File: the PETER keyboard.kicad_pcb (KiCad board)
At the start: 2 copper layers, 241.6 x 96.9 mm, 141 parts, among them J1 USB_C_Receptacle_USB2.0, SW1 RotaryEncoder_Switch, SW12 RotaryEncoder_Switch, SW2 SW_Push, U1 ATmega32U4-M, Y1 Crystal_GND24_Small

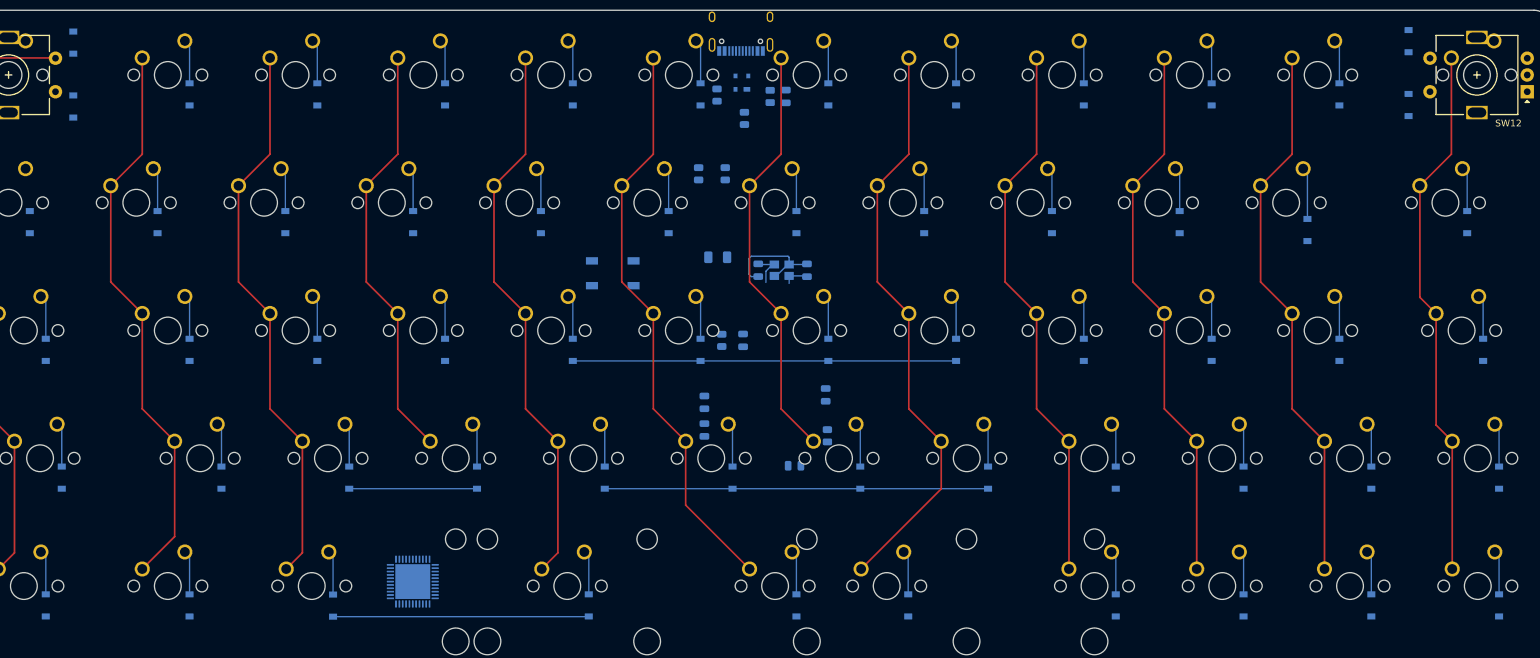
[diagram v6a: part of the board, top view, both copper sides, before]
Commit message: placed MCU and USB for automatic routing
also assigned row and col to MCU
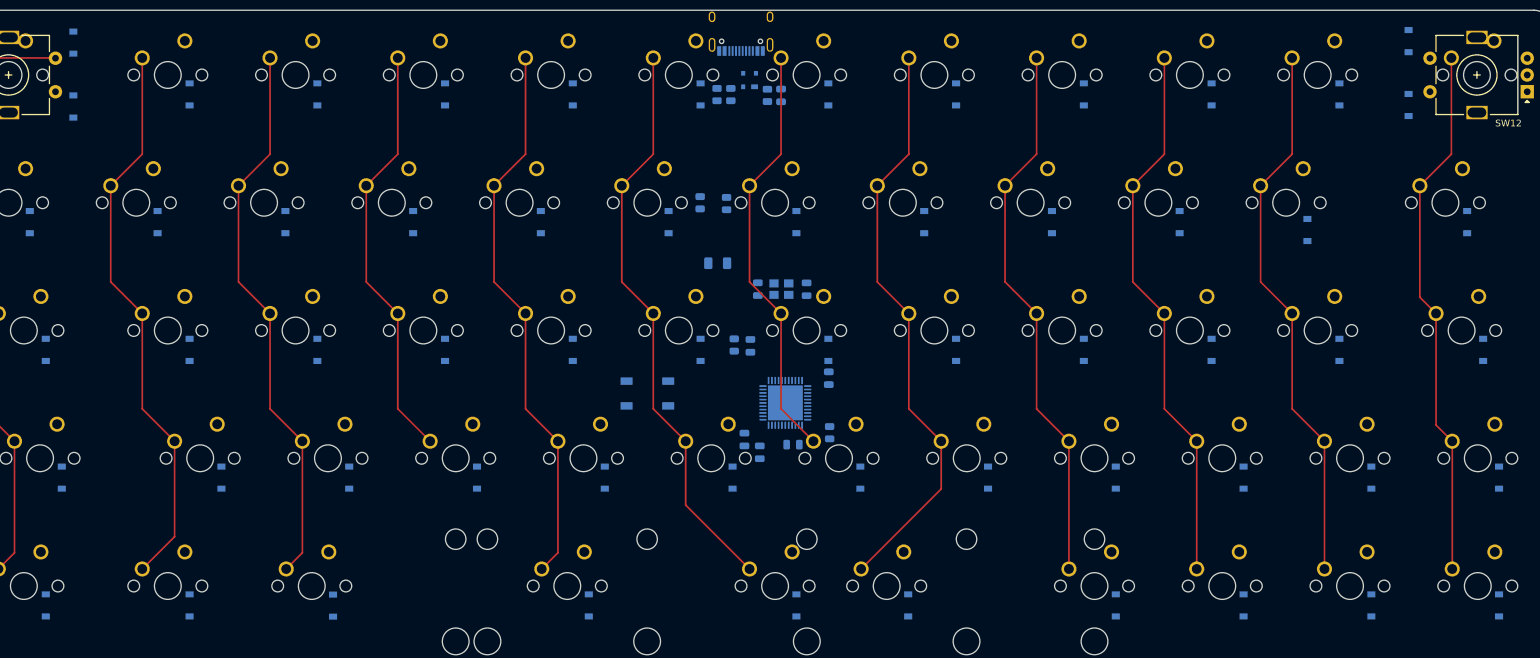
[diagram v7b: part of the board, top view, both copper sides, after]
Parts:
- moved U1 61.6 mm to (150.7, 105.5)
- moved SW2 18.7 mm to (130.2, 104.1)
- moved C_Decoupler4 8.90 mm to (146.9, 112.9)
- moved C_UCAP1 8.14 mm to (144.7, 111.0)
- moved R_USB4 4.45 mm to (142.0, 75.8)
- moved R_USB3 4.32 mm to (138.0, 75.7)
- moved R_USB2 4.10 mm to (142.6, 59.6)
- moved C_Decoupler2 3.16 mm to (151.9, 111.8)
- moved C_crystal2 2.83 mm to (146.7, 88.6)
- moved Y1 2.83 mm to (150.2, 88.6)
- moved C_crystal1 2.83 mm to (153.9, 88.6)
- moved C_Decoupler3 2.53 mm to (157.2, 101.9)
- moved R_reset1 1.98 mm to (143.1, 96.9)
- moved C_Decoupler1 1.36 mm to (145.5, 97.0)
- moved D59 1.20 mm to (145.4, 57.4)
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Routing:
- net  ROW3: track 76.2 -> 0.00 mm
- net ROW2: track 57.2 -> 0.00 mm
- net ROW4: track 38.1 -> 0.00 mm
- net GND: track 17.1 -> 0.00 mm
- net Net-(D23-Pad2): track 7.76 -> 0.00 mm
- net Net-(D49-Pad2): track 6.62 -> 0.00 mm
- net Net-(D25-Pad2): track 6.62 -> 0.00 mm
- net Net-(D51-Pad2): track 6.61 -> 0.00 mm
- net Net-(D6-Pad2): track 6.61 -> 0.00 mm
- net Net-(D11-Pad2): track 6.61 -> 0.00 mm
- net Net-(D35-Pad2): track 6.61 -> 0.00 mm
- net Net-(D30-Pad2): track 6.61 -> 0.00 mm
- net Net-(D50-Pad2): track 6.61 -> 0.00 mm
- net Net-(D4-Pad2): track 6.61 -> 0.00 mm
- net Net-(D3-Pad2): track 6.61 -> 0.00 mm
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
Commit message: traces have been auto routed
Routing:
- net GND: track 0.00 -> 430.5 mm
- net ROW0: track 0.00 -> 309.4 mm
- net ROW2: track 0.00 -> 255.9 mm, vias 0 -> 2
- net ROTARY_A: track 0.00 -> 242.3 mm
- net ROTARY_B: track 0.00 -> 237.0 mm
- net ROW4: track 0.00 -> 217.1 mm
- net ROW1: track 0.00 -> 216.5 mm, vias 0 -> 2
- net  ROW3: track 0.00 -> 215.9 mm
- net +5V: track 0.00 -> 91.5 mm
- net Net-(R_USB3-Pad2): track 0.00 -> 51.8 mm, vias 0 -> 2
- net Net-(R_USB4-Pad2): track 0.00 -> 50.9 mm, vias 0 -> 2
- net VCC: track 0.00 -> 40.7 mm
- net D+: track 0.00 -> 34.7 mm
- net D-: track 0.00 -> 30.2 mm
- net Net-(R_USBSHIELD1-Pad1): track 0.00 -> 26.1 mm
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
